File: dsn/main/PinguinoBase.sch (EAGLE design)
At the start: 27 parts, among them IC1 7805, Q1 20MHz, X1 

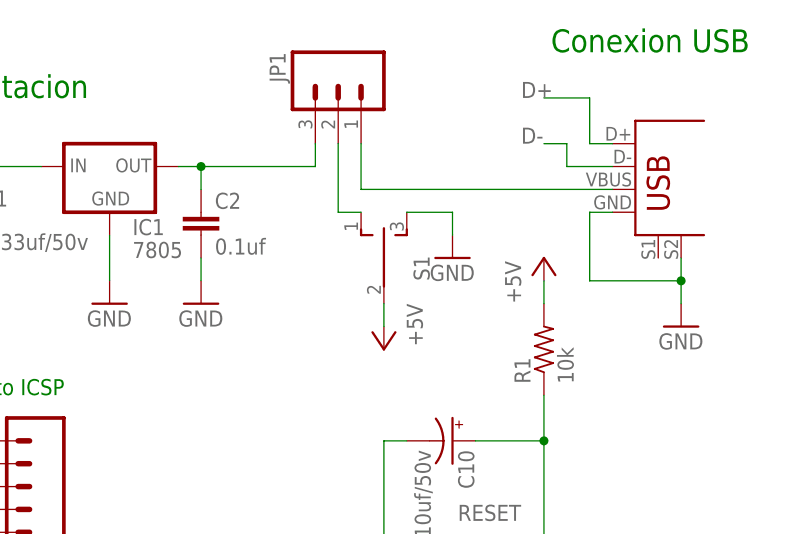
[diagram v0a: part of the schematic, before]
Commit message: Update R3.5
Nueva versión de PinguinoBase, a su versión 3.5, algunas modificaciones
de forma, reorganización de componentes, como el Cristal, capacitores,
eliminado switch de encendido, reorganizado de pistas.
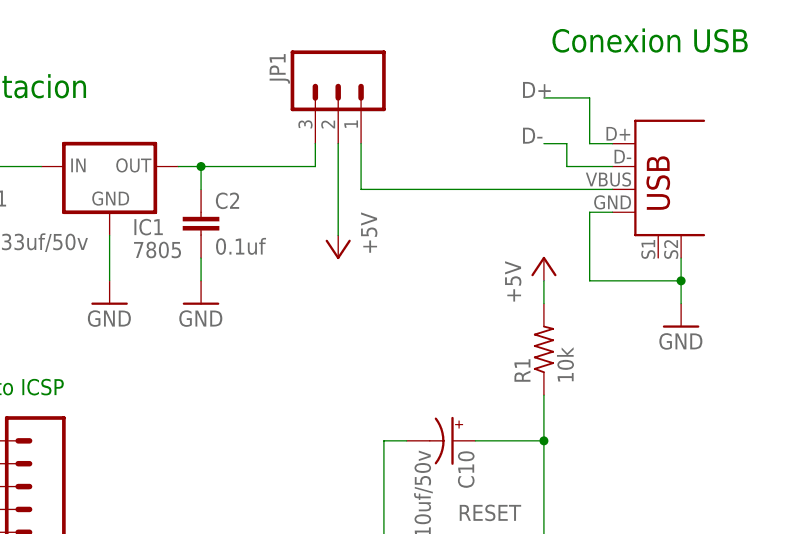
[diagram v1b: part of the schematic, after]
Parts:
- removed S1: TL39YOSWITCH_2_ESTADOS, aasanchez:TL39YOSWITCH_2_ESTADOS
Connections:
- removed net N$10: JP1.2, S1.O
- net +5V: now also JP1.2; no longer S1.P
- net GND: no longer S1.S
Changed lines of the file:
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@@
 <?xml version="1.0" encoding="utf-8"?>
 <!DOCTYPE eagle SYSTEM "eagle.dtd">
-<eagle version="6.1">
+<eagle version="6.4">
 <drawing>
 <settings>
@@
 <setting verticaltext="up"/>
 </settings>
-<grid distance="0.05" unitdist="inch" unit="inch" style="lines" multiple="1" display="yes" altdistance="0.01" altunitdist="inch" altunit="inch"/>
+<grid distance="0.1" unitdist="inch" unit="inch" style="lines" multiple="1" display="no" altdistance="0.01" altunitdist="inch" altunit="inch"/>
 <layers>
 <layer number="1" name="Top" color="4" fill="1" visible="no" active="no"/>
@@
 <part name="R2" library="resistor" deviceset="R-US_" device="0207/7" value="470"/>
 <part name="RUN" library="led" deviceset="LED" device="3MM" value="green"/>
-<part name="GND13" library="SparkFun" deviceset="GND" device=""/>
 <part name="C8" library="SparkFun" deviceset="CAP_POL" device="PTH2" value="0.22uf/50v"/>
 <part name="LOGO1" library="OSHW" deviceset="OSHW_LOGO_FILL" device="X0200-NT"/>
 <part name="JP2" library="SparkFun" deviceset="M06" device="LONGPADS" value=" "/>
-<part name="S1" library="aasanchez" deviceset="TL39YO" device="SWITCH_2_ESTADOS" value=""/>
 <part name="C2" library="SparkFun" deviceset="CAP" device="PTH2" value="0.1uf"/>
 <part name="JP3" library="SparkFun" deviceset="M08" device="LONGPADS" value=" "/>
@@
 <instance part="GND6" gate="1" x="53.34" y="99.06"/>
 <instance part="JP1" gate="G$1" x="15.24" y="127" rot="MR270"/>
-<instance part="P+2" gate="1" x="20.32" y="96.52" rot="R180"/>
+<instance part="P+2" gate="1" x="15.24" y="106.68" rot="R180"/>
 <instance part="18F4550" gate="G$1" x="5.08" y="30.48"/>
 <instance part="P+3" gate="1" x="-38.1" y="30.48" rot="R90"/>
@@
 <instance part="R2" gate="G$1" x="-48.26" y="53.34" rot="R90"/>
 <instance part="RUN" gate="G$1" x="-48.26" y="66.04"/>
-<instance part="GND13" gate="1" x="27.94" y="106.68"/>
 <instance part="C8" gate="G$1" x="-45.72" y="3.81"/>
 <instance part="LOGO1" gate="G$1" x="30.48" y="-2.54"/>
 <instance part="JP2" gate="G$1" x="-20.32" y="81.28" rot="R180"/>
-<instance part="S1" gate="BEF1" x="20.32" y="106.68"/>
 <instance part="C2" gate="G$1" x="0" y="109.22"/>
 <instance part="JP3" gate="G$1" x="-81.28" y="48.26" rot="MR180"/>
@@
 </segment>
 <segment>
-<wire x1="22.86" y1="111.76" x2="27.94" y2="111.76" width="0.1524" layer="91"/>
-<wire x1="27.94" y1="111.76" x2="27.94" y2="109.22" width="0.1524" layer="91"/>
-<pinref part="GND13" gate="1" pin="GND"/>
-<pinref part="S1" gate="BEF1" pin="S"/>
-</segment>
-<segment>
 <wire x1="-45.72" y1="-1.27" x2="-45.72" y2="-6.35" width="0.1524" layer="91"/>
 <pinref part="C8" gate="G$1" pin="-"/>
@@
 </segment>
 <segment>
-<wire x1="20.32" y1="101.6" x2="20.32" y2="99.06" width="0.1524" layer="91"/>
-<pinref part="S1" gate="BEF1" pin="P"/>
-<pinref part="P+2" gate="1" pin="+5V"/>
-</segment>
-<segment>
 <wire x1="-48.26" y1="68.58" x2="-48.26" y2="71.12" width="0.1524" layer="91"/>
 <pinref part="RUN" gate="G$1" pin="A"/>
@@
 <pinref part="P+1" gate="1" pin="+5V"/>
 <pinref part="C3" gate="G$1" pin="1"/>
+</segment>
+<segment>
+<wire x1="15.24" y1="109.22" x2="15.24" y2="119.38" width="0.1524" layer="91"/>
+<pinref part="JP1" gate="G$1" pin="2"/>
+<pinref part="P+2" gate="1" pin="+5V"/>
 </segment>
 </net>
@@
 </segment>
 </net>
-<net name="N$10" class="0">
-<segment>
-<wire x1="17.78" y1="111.76" x2="15.24" y2="111.76" width="0.1524" layer="91"/>
-<wire x1="15.24" y1="111.76" x2="15.24" y2="119.38" width="0.1524" layer="91"/>
-<pinref part="JP1" gate="G$1" pin="2"/>
-<pinref part="S1" gate="BEF1" pin="O"/>
-</segment>
-</net>

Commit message: Algunos cambios
Cambios simples en el diseño
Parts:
- removed C10: 10uf/50v, SparkFun:CAP_POLPTH2
- added C7: 0.1uf, SparkFun:CAPPTH2
- C1: value 0.33uf/50v -> 0.1uf; device SparkFun:CAP_POLPTH2 -> SparkFun:CAPPTH2
- C3, C4: value 0.1uf -> 22pf
- C5: value 22pf -> 0.22uf/50v; device SparkFun:CAPPTH2 -> SparkFun:CAP_POLPTH2
- C6: value 22pf -> 0.33uf/50v; device SparkFun:CAPPTH2 -> SparkFun:CAP_POLPTH2
- C8: value 0.22uf/50v -> 10uf/50v
- JP1: device SparkFun:M03LONGPADS -> SparkFun:M08LONGPADS
- JP2: device SparkFun:M06LONGPADS -> SparkFun:M08LONGPADS
- JP3: device SparkFun:M08LONGPADS -> SparkFun:M06LONGPADS
- JP4: device SparkFun:M08LONGPADS -> SparkFun:M03LONGPADS
- R1: value 10k -> 470
- R2: value 470 -> 10k
- renumbered U$1 to USB
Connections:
- net +5V: now also C1.1, C2.1, JP2.1, JP3.2, JP4.2, R2.2; no longer C3.1, C4.1, JP1.2, JP2.2, JP4.1, R1.2
- net GND: now also C1.2, C5.-, C6.-, C7.2, JP2.2, JP3.3; no longer C1.-, C10.-, C5.2, C6.2, JP2.3, JP4.2
- net N$1: now also C3.1; no longer C5.1
- net N$2: now also C6.+; no longer C1.+
- net N$3: now also C7.1, JP4.3; no longer C2.1, JP1.3
- net N$4: now also JP4.1; no longer JP1.1
- net N$5: now also C4.1; no longer C6.1
- net N$6: now also C5.+; no longer C8.+
- net N$7: now also R1.2; no longer R2.2
- net N$8: now also R1.1; no longer R2.1
- net PIN10: now also JP2.4; no longer JP4.4
- net PIN11: now also JP2.5; no longer JP4.5
- net PIN12: now also JP2.6; no longer JP4.6
- net PIN13: now also JP1.1; no longer JP3.1
- net PIN14: now also JP1.2; no longer JP3.2
- net PIN15: now also JP1.3; no longer JP3.3
- net PIN16: now also JP1.4; no longer JP3.4
- net PIN17: now also JP1.5; no longer JP3.5
- net PIN18: now also JP1.6; no longer JP3.6
- net PIN19: now also JP1.7; no longer JP3.7
- net PIN20: now also JP1.8; no longer JP3.8
- net PIN21: now also JP2.7; no longer JP4.7
- net PIN22: now also JP2.8; no longer JP4.8
- net PIN6: now also JP3.5; no longer JP2.5
- net PIN7: now also JP3.4; no longer JP2.4
- net RESET: now also C8.+, JP2.3, JP3.1, R2.1; no longer C10.+, JP2.1, JP4.3, R1.1
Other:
- moved on the sheet: C2, C3, C4, C8, R1, R2

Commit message: some Fixes
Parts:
- removed LOGO1: OSHW_LOGO_FILLX0200-NT, OSHW:OSHW_LOGO_FILLX0200-NT
- added CC_TEXT1: CREATIVE_COMMONS, SparkFun-Aesthetics:CREATIVE_COMMONS
- added LOGO2: OSHW-LOGOL, SparkFun-Aesthetics:OSHW-LOGOL
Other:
- note added: "Alexis -PaX- Sánchez"

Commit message: Renumeracion de Componentes, mejoras en el BOM, y correccion a detalles esteticos en el Board
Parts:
- removed JP6: (no value), SparkFun:M08LONGPADS
- added ICSP: (no value), SparkFun:M06LONGPADS
- C1: value 0.1uf -> 10uf/50v; device SparkFun:CAPPTH2 -> SparkFun:CAP_POLPTH2
- C3: value 22pf -> 0.33uf/50v; device SparkFun:CAPPTH2 -> SparkFun:CAP_POLPTH2
- C4: value 22pf -> 0.22uf/50v; device SparkFun:CAPPTH2 -> SparkFun:CAP_POLPTH2
- C5: value 0.22uf/50v -> 22pf; device SparkFun:CAP_POLPTH2 -> SparkFun:CAPPTH2
- C6: value 0.33uf/50v -> 22pf; device SparkFun:CAP_POLPTH2 -> SparkFun:CAPPTH2
- C8: value 10uf/50v -> 0.1uf; device SparkFun:CAP_POLPTH2 -> SparkFun:CAPPTH2
- JP3: device SparkFun:M06LONGPADS -> SparkFun:M03LONGPADS
- JP4: device SparkFun:M03LONGPADS -> SparkFun:M08LONGPADS
- R1: value 470 -> 10k
- R2: value 10k -> 470
- renumbered LOGO2 to LOGO1
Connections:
- net +5V: now also C7.1, C8.1, ICSP.2, JP5.1, R1.2; no longer C1.1, C2.1, JP2.1, JP4.2, R2.2
- net GND: now also C1.-, C3.-, C4.-, C5.2, C6.2, C8.2, ICSP.3, JP5.2; no longer C1.2, C3.2, C4.2, C5.-, C6.-, C8.-, JP2.2, JP3.3
- net N$1: now also C5.1; no longer C3.1
- net N$2: now also C3.+; no longer C6.+
- net N$3: now also C2.1, JP3.3; no longer C7.1, JP4.3
- net N$4: now also JP3.1; no longer JP4.1
- net N$5: now also C6.1; no longer C4.1
- net N$6: now also C4.+; no longer C5.+
- net N$7: now also R2.2; no longer R1.2
- net N$8: now also R2.1; no longer R1.1
- net PIN0: now also JP1.1; no longer JP5.1
- net PIN1: now also JP1.2; no longer JP5.2
- net PIN10: now also JP5.4; no longer JP2.4
- net PIN11: now also JP5.5; no longer JP2.5
- net PIN12: now also JP5.6; no longer JP2.6
- net PIN13: now also JP4.1; no longer JP1.1
- net PIN14: now also JP4.2; no longer JP1.2
- net PIN15: now also JP4.3; no longer JP1.3
- net PIN16: now also JP4.4; no longer JP1.4
- net PIN17: now also JP4.5; no longer JP1.5
- net PIN18: now also JP4.6; no longer JP1.6
- net PIN19: now also JP4.7; no longer JP1.7
- net PIN2: now also JP1.3; no longer JP5.3
- net PIN20: now also JP4.8; no longer JP1.8
- net PIN21: now also JP5.7; no longer JP2.7
- net PIN22: now also JP5.8; no longer JP2.8
- net PIN23: now also JP2.1; no longer JP6.1
- net PIN24: now also JP2.2; no longer JP6.2
- net PIN25: now also JP2.5; no longer JP6.5
- net PIN26: now also JP2.6; no longer JP6.6
- net PIN27: now also JP2.7; no longer JP6.7
- net PIN28: now also JP2.8; no longer JP6.8
- net PIN3: now also JP1.4; no longer JP5.4
- net PIN4: now also JP1.5; no longer JP5.5
- net PIN5: now also JP1.6; no longer JP5.6
- net PIN6: now also ICSP.5, JP1.7; no longer JP3.5, JP5.7
- net PIN7: now also ICSP.4, JP1.8; no longer JP3.4, JP5.8
- net PIN8: now also JP2.3; no longer JP6.3
- net PIN9: now also JP2.4; no longer JP6.4
- net RESET: now also C1.+, ICSP.1, JP5.3, R1.1; no longer C8.+, JP2.3, JP3.1, R2.1
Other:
- moved on the sheet: C2, C7, JP1, JP2, JP5, Q1, R1, R2
